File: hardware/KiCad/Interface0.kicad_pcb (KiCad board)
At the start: 2 copper layers, 75 x 85 mm, 9 parts, among them J1 RPi_GPIO, U1 XC9572XL-VQ64

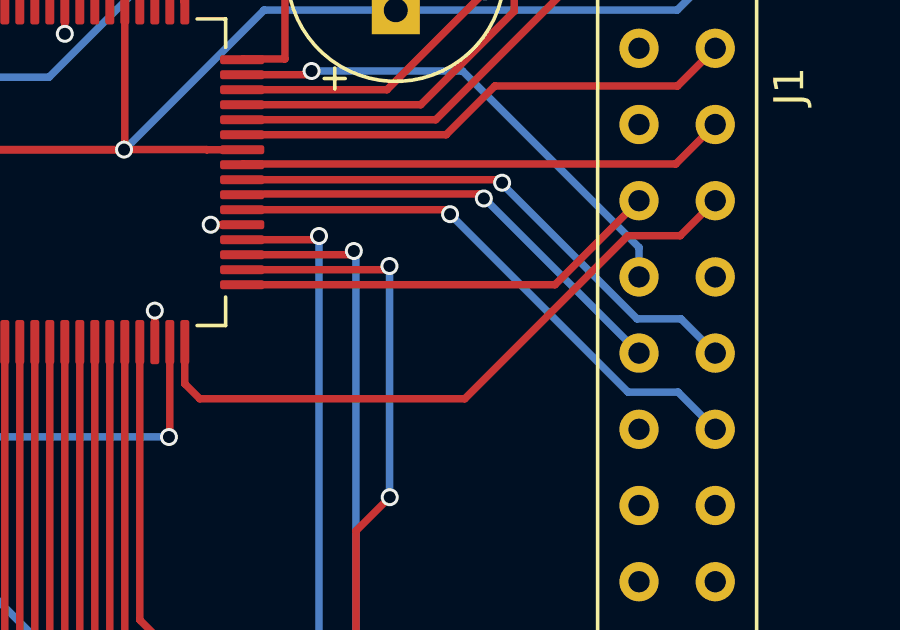
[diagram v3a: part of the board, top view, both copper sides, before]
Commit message: Use custom IO protocol
Use GPCLK1 as a master clock
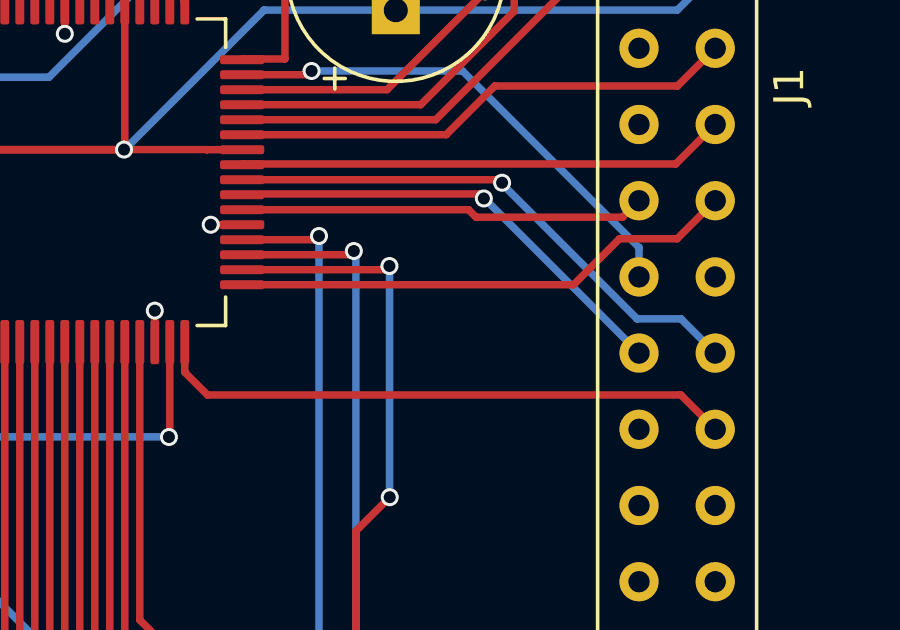
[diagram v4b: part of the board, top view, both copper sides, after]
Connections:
- net /SPI_MISO renamed /MISO
- net /SPI_MOSI renamed /MOSI
- J1 pad 23: /SPI_CLK -> /IO_CLK
- J1 pad 24: /SPI_CE0 -> /IO
- J1 pad 26: /GPIO4 -> /GPIO3
- J1 pad 27: /GPIO2 -> /GPIO1
- J1 pad 28: /GPIO3 -> /GPIO2
- J1 pad 29: /GPIO1 -> /MASTER_CLK
- U1 pad 16: /SPI_CLK -> /MASTER_CLK
- U1 pad 17: /SPI_CE0 -> /IO_CLK
- U1 pad 22: /GPIO1 -> /IO
- U1 pad 23: /GPIO3 -> /GPIO2
- U1 pad 24: /GPIO2 -> /GPIO1
- U1 pad 31: /GPIO4 -> /GPIO3
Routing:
- net /SPI_CLK: track 22.0 -> 0.00 mm
- net /MASTER_CLK: track 0.00 -> 19.5 mm
- net /IO_CLK: track 0.00 -> 16.9 mm
- net /GPIO4: track 16.7 -> 0.00 mm, vias 1 -> 0
- net /SPI_CE0: track 14.4 -> 0.00 mm
- net /IO: track 0.00 -> 13.6 mm
- net /GPIO2: track 18.2 -> 14.7 mm
- net /GPIO3: track 14.7 -> 16.7 mm
- net /GPIO1: track 18.8 -> 18.2 mm

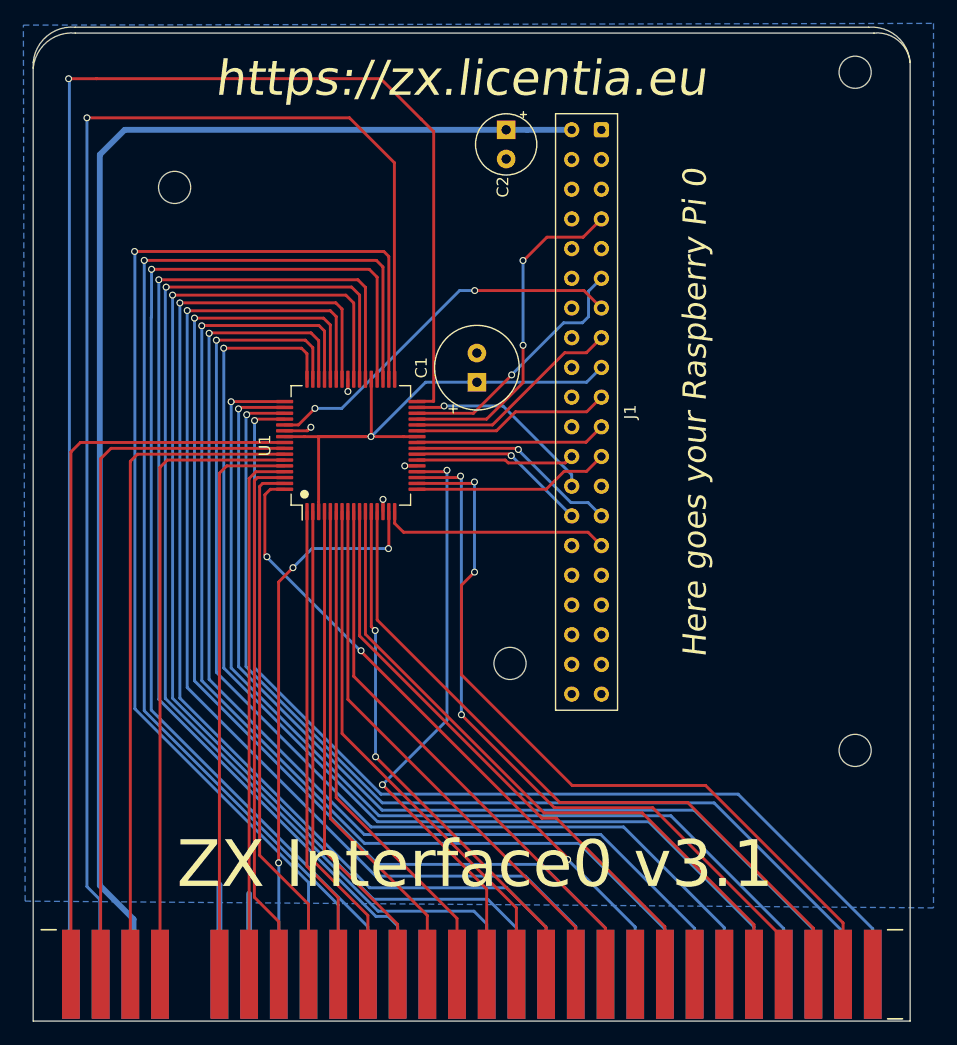
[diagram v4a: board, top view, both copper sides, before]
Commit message: Nuke HALT & RFSH and connect them to RPi
Add first verilog implementation
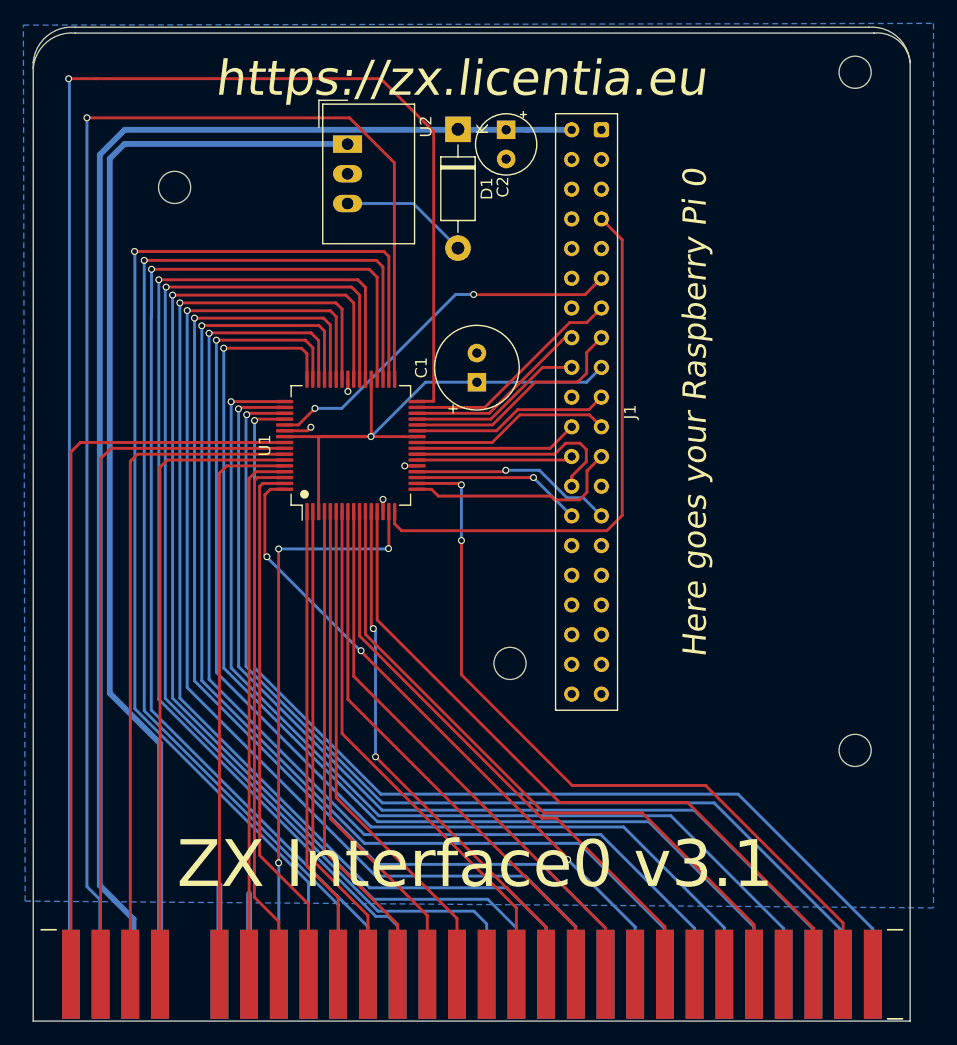
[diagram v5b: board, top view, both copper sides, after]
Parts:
- added D1: 1N4001, Diode_THT:D_DO-41_SOD81_P10.16mm_Horizontal, F.Cu at (57.3, 24.3)
- added U2: TSR_1-2450, Converter_DCDC:Converter_DCDC_TRACO_TSR-1_THT, F.Cu at (47.9, 25.6)
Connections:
- J1 pad 11: /TCK -> /TDO
- J1 pad 13: /TDO -> /GPIO3
- J1 pad 16: unconnected-(J1-Pad16) -> /TCK
- J1 pad 18: unconnected-(J1-Pad18) -> /TMS
- J1 pad 22: unconnected-(J1-Pad22) -> /GPIO1
- J1 pad 26: /GPIO3 -> /GPIO2
- J1 pad 27: /GPIO1 -> /GPIO4
- J1 pad 28: /GPIO2 -> /GPIO5
- J1 pad 29: /MASTER_CLK -> unconnected-(J1-Pad29)
- J1 pad 7: /TMS -> /MASTER_CLK
- U1 pad 19: /RFSH -> /GPIO5
- U1 pad 20: /HALT -> /GPIO4
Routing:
- net +9V: track 0.00 -> 92.2 mm
- net /RFSH: track 62.8 -> 0.00 mm, vias 2 -> 0
- net /HALT: track 51.7 -> 0.00 mm, vias 2 -> 0
- net /MASTER_CLK: track 19.5 -> 46.9 mm
- net /GPIO4: track 0.00 -> 17.4 mm, vias 0 -> 1
- net /GPIO5: track 0.00 -> 14.6 mm, vias 0 -> 1
- net /TMS: track 29.0 -> 15.1 mm, vias 2 -> 0
- net Net-(U2-Pad3): track 0.00 -> 11.0 mm
- net /TCK: track 21.8 -> 15.9 mm, vias 1 -> 0
- net /GPIO1: track 18.2 -> 14.0 mm, vias 1 -> 0
- net /GPIO2: track 14.7 -> 18.8 mm, vias 1 -> 0
- net /GPIO3: track 16.7 -> 19.3 mm, vias 1 -> 0
- net /A10: track 67.7 -> 65.9 mm
- net /IO_CLK: track 16.9 -> 18.8 mm
- net /CLK: track 47.3 -> 49.0 mm
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
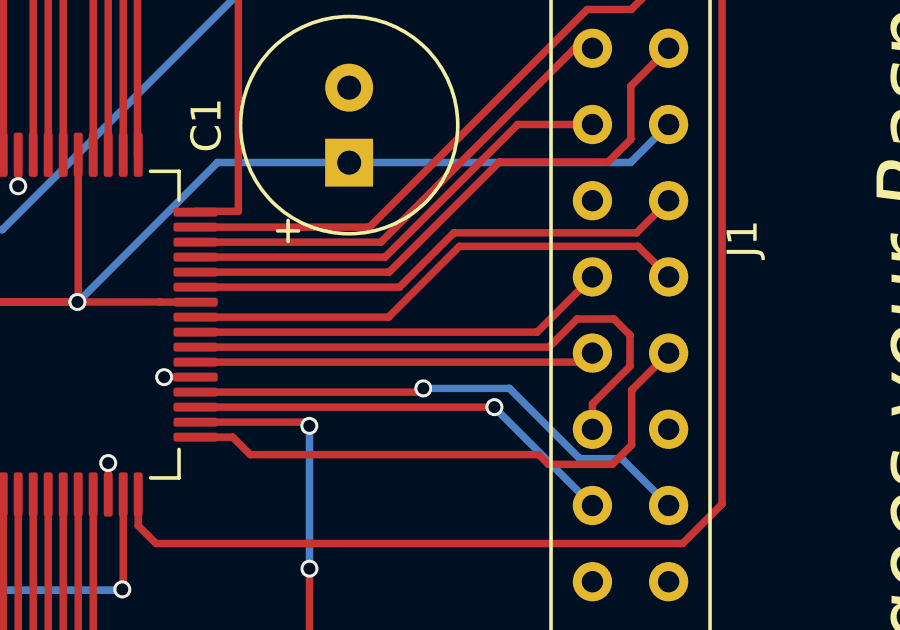
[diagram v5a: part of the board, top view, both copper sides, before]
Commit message: Swap p25 with p23 to free one FB from FB4
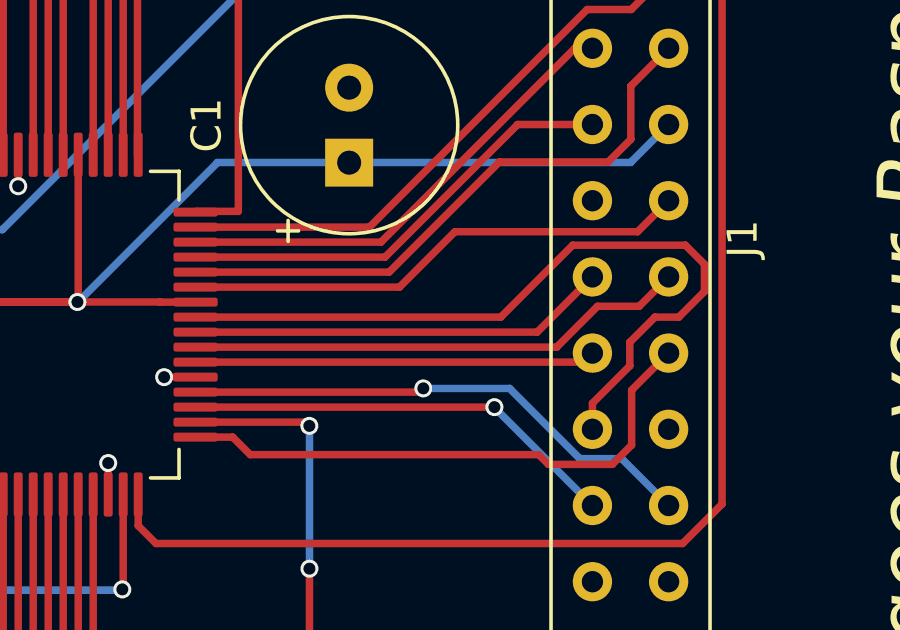
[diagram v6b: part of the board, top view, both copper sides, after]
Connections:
- U1 pad 23: /GPIO2 -> /MISO
- U1 pad 25: /MISO -> /GPIO2
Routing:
- net /GPIO2: track 18.8 -> 25.7 mm
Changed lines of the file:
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@@
   (net 87 "/GPIO5")
   (net 88 "/GPIO4")
-  (net 89 "Net-(U2-Pad3)")
+  (net 89 "Net-(D1-Pad2)")
   (footprint "" (layer "F.Cu")
     (at 33.094 29.308 90)
@@
       (net 4 "GND") (pinfunction "GND") (pintype "power_in"))
     (pad "3" thru_hole oval (at 5.08 0 270) (size 1.5 2.5) (drill 1) (layers *.Cu *.Mask)
-      (net 89 "Net-(U2-Pad3)") (pinfunction "Vout") (pintype "power_out"))
+      (net 89 "Net-(D1-Pad2)") (pinfunction "Vout") (pintype "power_out"))
     (model "${KICAD6_3DMODEL_DIR}/Converter_DCDC.3dshapes/Converter_DCDC_TRACO_TSR-1_THT.wrl"
       (offset (xyz 0 0 0))
@@
       (net 82 "/IO") (pinfunction "P22") (pintype "bidirectional"))
     (pad "23" smd roundrect (at -0.75 5.6625 90) (size 0.3 1.475) (layers "F.Cu" "F.Paste" "F.Mask") (roundrect_rratio 0.25)
-      (net 76 "/GPIO2") (pinfunction "P23") (pintype "bidirectional"))
+      (net 6 "/MISO") (pinfunction "P23") (pintype "bidirectional"))
     (pad "24" smd roundrect (at -0.25 5.6625 90) (size 0.3 1.475) (layers "F.Cu" "F.Paste" "F.Mask") (roundrect_rratio 0.25)
       (net 75 "/GPIO1") (pinfunction "P24") (pintype "bidirectional"))
     (pad "25" smd roundrect (at 0.25 5.6625 90) (size 0.3 1.475) (layers "F.Cu" "F.Paste" "F.Mask") (roundrect_rratio 0.25)
-      (net 6 "/MISO") (pinfunction "P25") (pintype "bidirectional"))
+      (net 76 "/GPIO2") (pinfunction "P25") (pintype "bidirectional"))
     (pad "26" smd roundrect (at 0.75 5.6625 90) (size 0.3 1.475) (layers "F.Cu" "F.Paste" "F.Mask") (roundrect_rratio 0.25)
       (net 1 "+3V3") (pinfunction "VCCIO") (pintype "power_in"))
@@
       (net 31 "+5V") (pinfunction "K") (pintype "passive"))
     (pad "2" thru_hole oval (at 10.16 0 270) (size 2.2 2.2) (drill 1.1) (layers *.Cu *.Mask)
-      (net 89 "Net-(U2-Pad3)") (pinfunction "A") (pintype "passive"))
+      (net 89 "Net-(D1-Pad2)") (pinfunction "A") (pintype "passive"))
     (model "${KICAD6_3DMODEL_DIR}/Diode_THT.3dshapes/D_DO-41_SOD81_P10.16mm_Horizontal.wrl"
       (offset (xyz 0 0 0))
@@
   (segment (start 39.466 96.609) (end 39.466 89.716) (width 0.5) (layer "B.Cu") (net 4))
   (segment (start 36.926 96.609) (end 36.926 88.954) (width 0.5) (layer "B.Cu") (net 4))
-  (segment (start 69.596 47.244) (end 68.52452 48.31548) (width 0.25) (layer "F.Cu") (net 5))
+  (segment (start 62.472 48.278) (end 60.625153 50.124847) (width 0.25) (layer "F.Cu") (net 5))
+  (segment (start 69.596 47.244) (end 68.562 48.278) (width 0.25) (layer "F.Cu") (net 5))
   (segment (start 60.625153 50.124847) (end 53.82772 50.124847) (width 0.25) (layer "F.Cu") (net 5))
-  (segment (start 68.52452 48.31548) (end 62.434521 48.31548) (width 0.25) (layer "F.Cu") (net 5))
-  (segment (start 62.434521 48.31548) (end 60.625153 50.124847) (width 0.25) (layer "F.Cu") (net 5))
-  (segment (start 53.82772 51.124847) (end 60.260871 51.124847) (width 0.25) (layer "F.Cu") (net 6))
-  (segment (start 60.260871 51.124847) (end 62.620718 48.765) (width 0.25) (layer "F.Cu") (net 6))
-  (segment (start 62.620718 48.765) (end 68.577 48.765) (width 0.25) (layer "F.Cu") (net 6))
-  (segment (start 68.577 48.765) (end 69.596 49.784) (width 0.25) (layer "F.Cu") (net 6))
+  (segment (start 68.562 48.278) (end 62.472 48.278) (width 0.25) (layer "F.Cu") (net 5))
+  (segment (start 65.865153 52.124847) (end 67.226489 50.763511) (width 0.25) (layer "F.Cu") (net 6))
+  (segment (start 53.82772 52.124847) (end 65.865153 52.124847) (width 0.25) (layer "F.Cu") (net 6))
+  (segment (start 67.226489 50.763511) (end 68.616489 50.763511) (width 0.25) (layer "F.Cu") (net 6))
+  (segment (start 68.616489 50.763511) (end 69.596 49.784) (width 0.25) (layer "F.Cu") (net 6))
   (segment (start 55.064847 55.124847) (end 55.649 55.709) (width 0.25) (layer "F.Cu") (net 7))
   (segment (start 67.719 56.033) (end 68.363 55.389) (width 0.25) (layer "F.Cu") (net 7))
@@
   (segment (start 65.215153 51.624847) (end 67.056 49.784) (width 0.25) (layer "F.Cu") (net 75))
   (segment (start 53.82772 51.624847) (end 65.215153 51.624847) (width 0.25) (layer "F.Cu") (net 75))
-  (segment (start 66.545 51.187) (end 67.773 51.187) (width 0.25) (layer "F.Cu") (net 76))
-  (segment (start 68.307 51.721) (end 68.307 52.767) (width 0.25) (layer "F.Cu") (net 76))
-  (segment (start 53.82772 52.124847) (end 65.607153 52.124847) (width 0.25) (layer "F.Cu") (net 76))
-  (segment (start 67.773 51.187) (end 68.307 51.721) (width 0.25) (layer "F.Cu") (net 76))
-  (segment (start 67.056 54.018) (end 67.056 54.864) (width 0.25) (layer "F.Cu") (net 76))
-  (segment (start 65.607153 52.124847) (end 66.545 51.187) (width 0.25) (layer "F.Cu") (net 76))
-  (segment (start 68.307 52.767) (end 67.056 54.018) (width 0.25) (layer "F.Cu") (net 76))
+  (segment (start 69.937 51.124) (end 69.14 51.124) (width 0.25) (layer "F.Cu") (net 76))
+  (segment (start 70.15552 48.72752) (end 70.789 49.361) (width 0.25) (layer "F.Cu") (net 76))
+  (segment (start 64.000153 51.124847) (end 66.39748 48.72752) (width 0.25) (layer "F.Cu") (net 76))
+  (segment (start 68.302 51.962) (end 68.302 52.75) (width 0.25) (layer "F.Cu") (net 76))
+  (segment (start 53.82772 51.124847) (end 64.000153 51.124847) (width 0.25) (layer "F.Cu") (net 76))
+  (segment (start 70.789 50.272) (end 69.937 51.124) (width 0.25) (layer "F.Cu") (net 76))
+  (segment (start 68.302 52.75) (end 67.056 53.996) (width 0.25) (layer "F.Cu") (net 76))
+  (segment (start 66.39748 48.72752) (end 70.15552 48.72752) (width 0.25) (layer "F.Cu") (net 76))
+  (segment (start 67.056 53.996) (end 67.056 54.864) (width 0.25) (layer "F.Cu") (net 76))
+  (segment (start 69.14 51.124) (end 68.302 51.962) (width 0.25) (layer "F.Cu") (net 76))
+  (segment (start 70.789 49.361) (end 70.789 50.272) (width 0.25) (layer "F.Cu") (net 76))
   (segment (start 59.625153 48.124847) (end 66.879 40.871) (width 0.25) (layer "F.Cu") (net 77))
   (segment (start 53.82772 48.124847) (end 59.625153 48.124847) (width 0.25) (layer "F.Cu") (net 77))
